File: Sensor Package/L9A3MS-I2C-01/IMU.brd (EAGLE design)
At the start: 38.1 x 25.5 mm, 15 parts

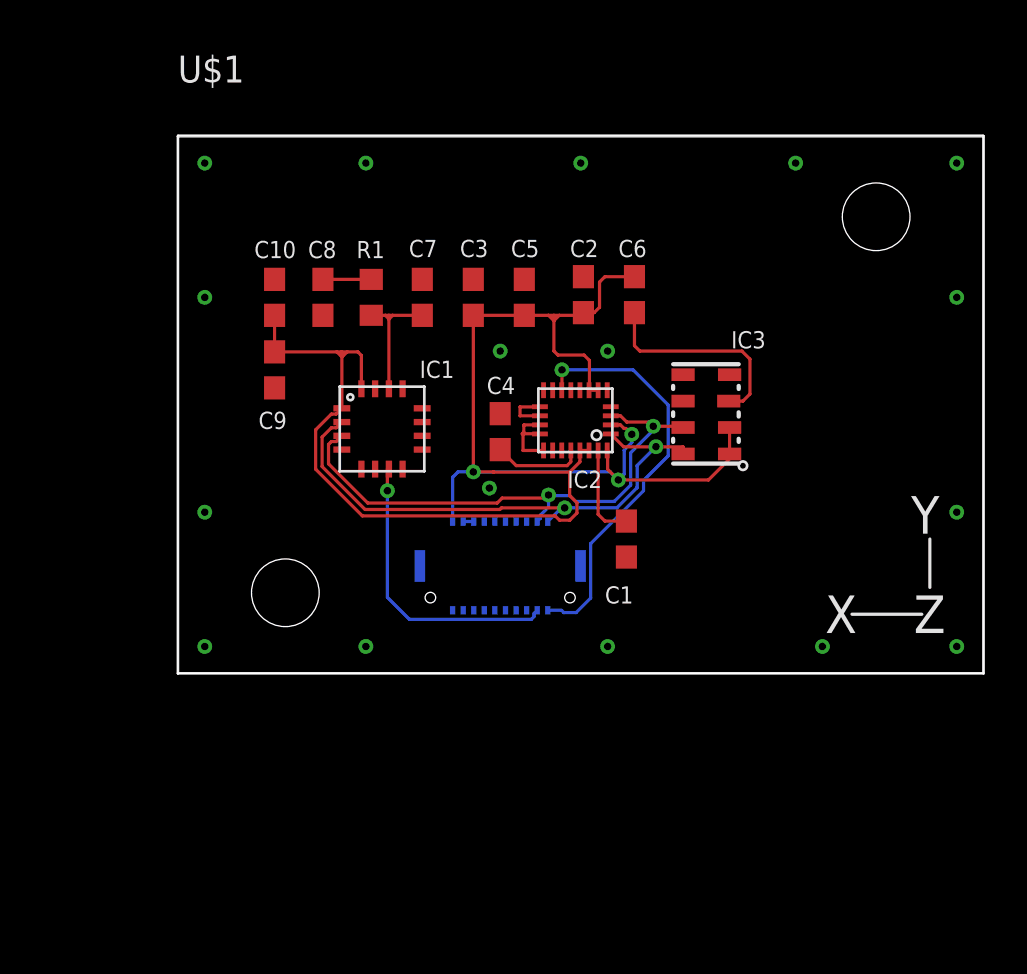
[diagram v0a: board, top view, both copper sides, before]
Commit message: Modified Libraries, Worked on STM32F3 Core
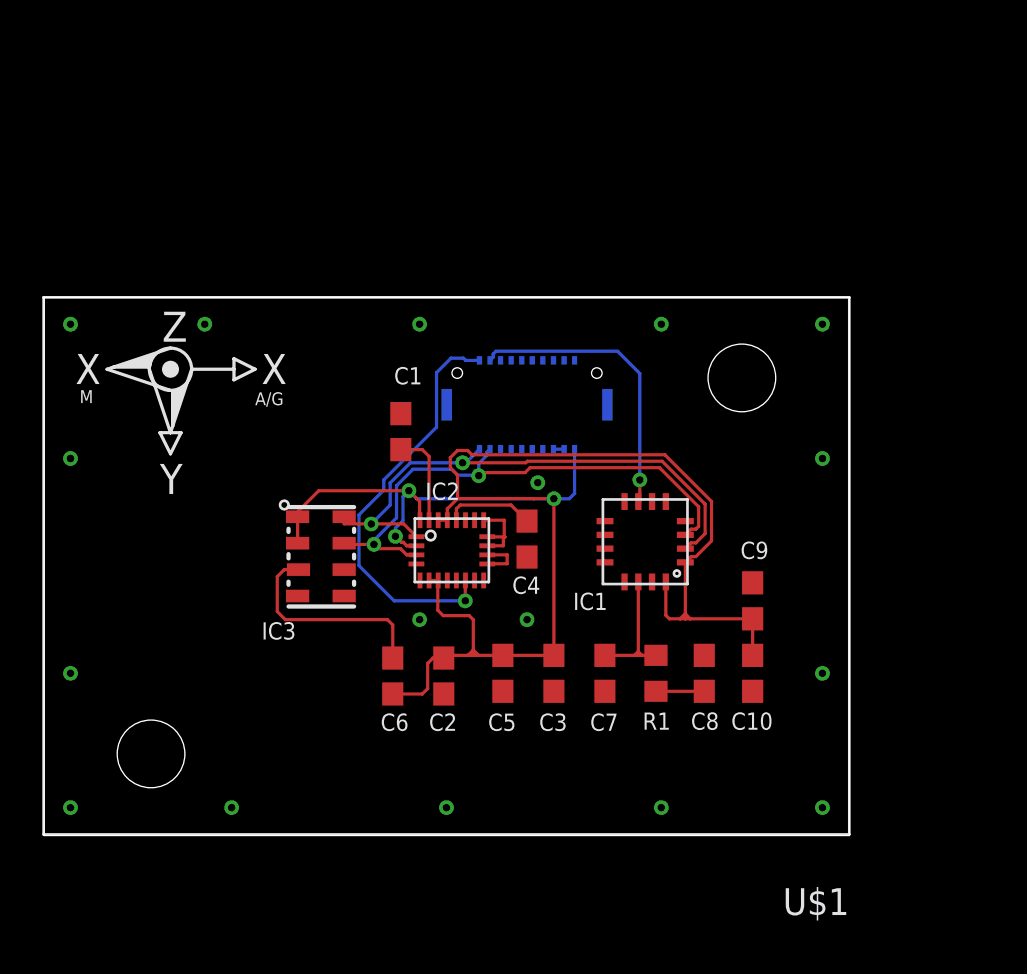
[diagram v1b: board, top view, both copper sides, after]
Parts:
- moved U$1 36.4 mm to (38.1, 25.4), turned to 180 degrees
- moved C10 28.8 mm to (33.5, 7.62), turned to 270 degrees
- moved C8 25.3 mm to (31.2, 7.62), turned to 270 degrees
- moved C9 25.1 mm to (33.5, 11.0), turned to 90 degrees
- moved R1 22.3 mm to (29.0, 7.62), turned to 270 degrees
- moved C6 21.4 mm to (16.5, 7.49), turned to 90 degrees
- moved C7 19.8 mm to (26.5, 7.62), turned to 90 degrees
- moved MS5611 19.5 mm to (13.1, 13.1), turned to 0 degrees
- moved C2 19.2 mm to (18.9, 7.49), turned to 90 degrees
- moved C3 18.2 mm to (24.1, 7.62), turned to 90 degrees
- moved C5 17.8 mm to (21.7, 7.62), turned to 90 degrees
- moved A3G4250D 13.5 mm to (28.4, 13.8), turned to 180 degrees
- moved C1 11.8 mm to (16.9, 19.1), turned to 270 degrees
- moved U$2 8.48 mm to (19.3, 13.4), turned to 90 degrees
- moved C4 5.24 mm to (22.9, 14.0), turned to 90 degrees
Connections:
- net GND: now also MS5611.4, MS5611.5
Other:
- board text added: "A/G"
- board text added: "Cal Poly Space Systems L3A9MS-I2C-02"
- board text added: "M"
- board text removed: "Cal Poly Space Systems L3A9MS-I2C-01"
